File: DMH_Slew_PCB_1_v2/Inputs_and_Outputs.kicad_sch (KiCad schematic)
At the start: 4 parts, among them J200 IDC_02x05, J4 TS_Jack_6.35mm_Sw, J50 Conn_01x06, J60 Conn_01x06

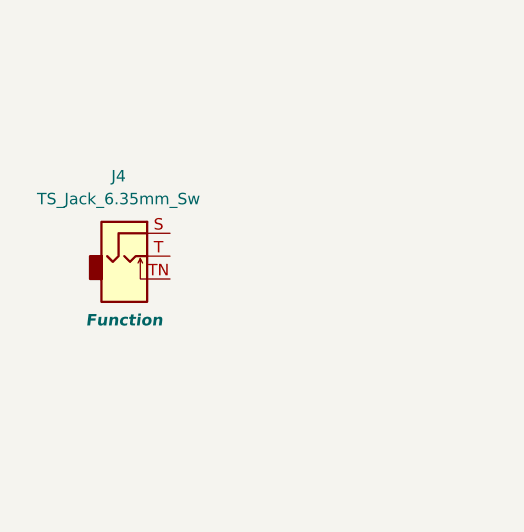
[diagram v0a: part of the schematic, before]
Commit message: Added state gate outputs circuit
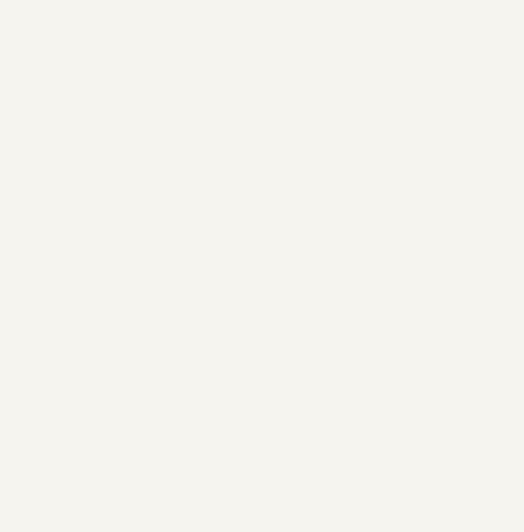
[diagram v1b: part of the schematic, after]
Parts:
- removed J4: TS_Jack_6.35mm_Sw, SynthStuff:CUI_MJ-63052A, symbol SynthStuff:TS_Jack_6.35mm_Sw
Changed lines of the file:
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@@
-		)
-	)
-	(symbol
-		(lib_id "SynthStuff:TS_Jack_6.35mm_Sw")
-		(at 25.4 101.6 0)
-		(unit 1)
-		(exclude_from_sim no)
-		(in_bom yes)
-		(on_board yes)
-		(dnp no)
-		(property "Reference" "J4"
-			(at 24.765 92.71 0)
-			(effects
-				(font
-					(size 1.27 1.27)
-				)
-			)
-		)
-		(property "Value" "TS_Jack_6.35mm_Sw"
-			(at 24.765 95.25 0)
-			(effects
-				(font
-					(size 1.27 1.27)
-				)
-			)
-		)
-		(property "Footprint" "SynthStuff:CUI_MJ-63052A"
-			(at 25.4 101.6 0)
-			(effects
-				(font
-					(size 1.27 1.27)
-				)
-				(hide yes)
-			)
-		)
-		(property "Datasheet" "~"
-			(at 25.4 101.6 0)
-			(effects
-				(font
-					(size 1.27 1.27)
-				)
-				(hide yes)
-			)
-		)
-		(property "Description" "Audio Jack, 2 Poles (Mono / TS), Switched T Pole (Normalling), 6.35mm, 1/4inch"
-			(at 25.4 101.6 0)
-			(effects
-				(font
-					(size 1.27 1.27)
-				)
-				(hide yes)
-			)
-		)
-		(property "Function" "Function"
-			(at 25.4 108.712 0)
-			(effects
-				(font
-					(size 1.27 1.27)
-					(thickness 0.254)
-					(bold yes)
-					(italic yes)
-				)
-			)
-		)
-		(pin "TN"
-		)
-		(pin "S"
-		)
-		(pin "T"
-		)
-		(instances
-			(project "DMH-Kosmo-5cm-PCB"
-				(path "/58f4306d-5387-4983-bb08-41a2313fd315/ce3fef8b-9f1d-4178-b50b-4a046c030679"
-					(reference "J4")
-					(unit 1)
-				)
-			)
 		)
 	)
